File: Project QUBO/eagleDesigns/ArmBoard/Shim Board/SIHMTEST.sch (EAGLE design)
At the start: 11 parts, among them U1 BME280

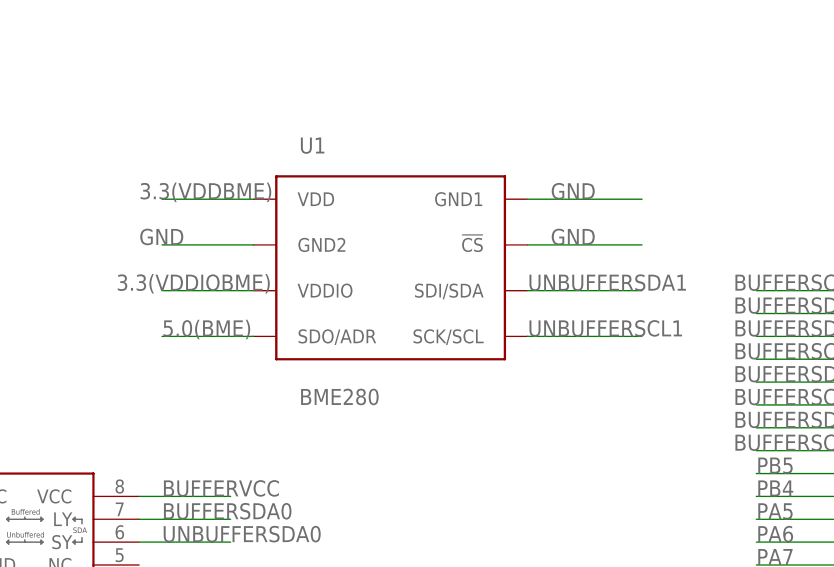
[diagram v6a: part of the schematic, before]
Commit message: 
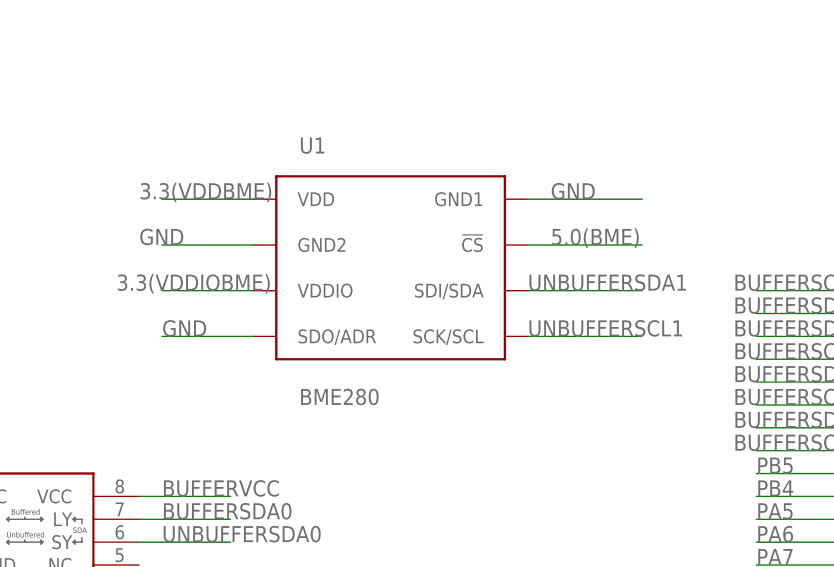
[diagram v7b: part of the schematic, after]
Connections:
- net 5.0(BME): now also U1.!CS; no longer U1.SDO/ADR
- net GND: now also U1.SDO/ADR; no longer U1.!CS
